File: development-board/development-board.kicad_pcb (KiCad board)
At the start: 2 copper layers, 153 x 77 mm, 103 parts, among them J1 East, J10 Ext_5V, J2 Screw_Terminal, J3 USB_B, J4 Keyboard, J5 Mouse, J6 Audio, J7 VGA, J8 West, J9 PinOut, Q1 MMBT3904, Q2 MMBT3904, Q3 S8050, Q4 S8050, SW1 Reset, SW2 Setup, SW3 Power, U1 LD1117S33, U2 FT2232HL, U3 93C46-WMN6TP, U4 LTV-817S, U5 LTV-817S, U6 MAX3486, U7 SN74CBT16292, U8 SN74CBT16292, Y1 12MHz

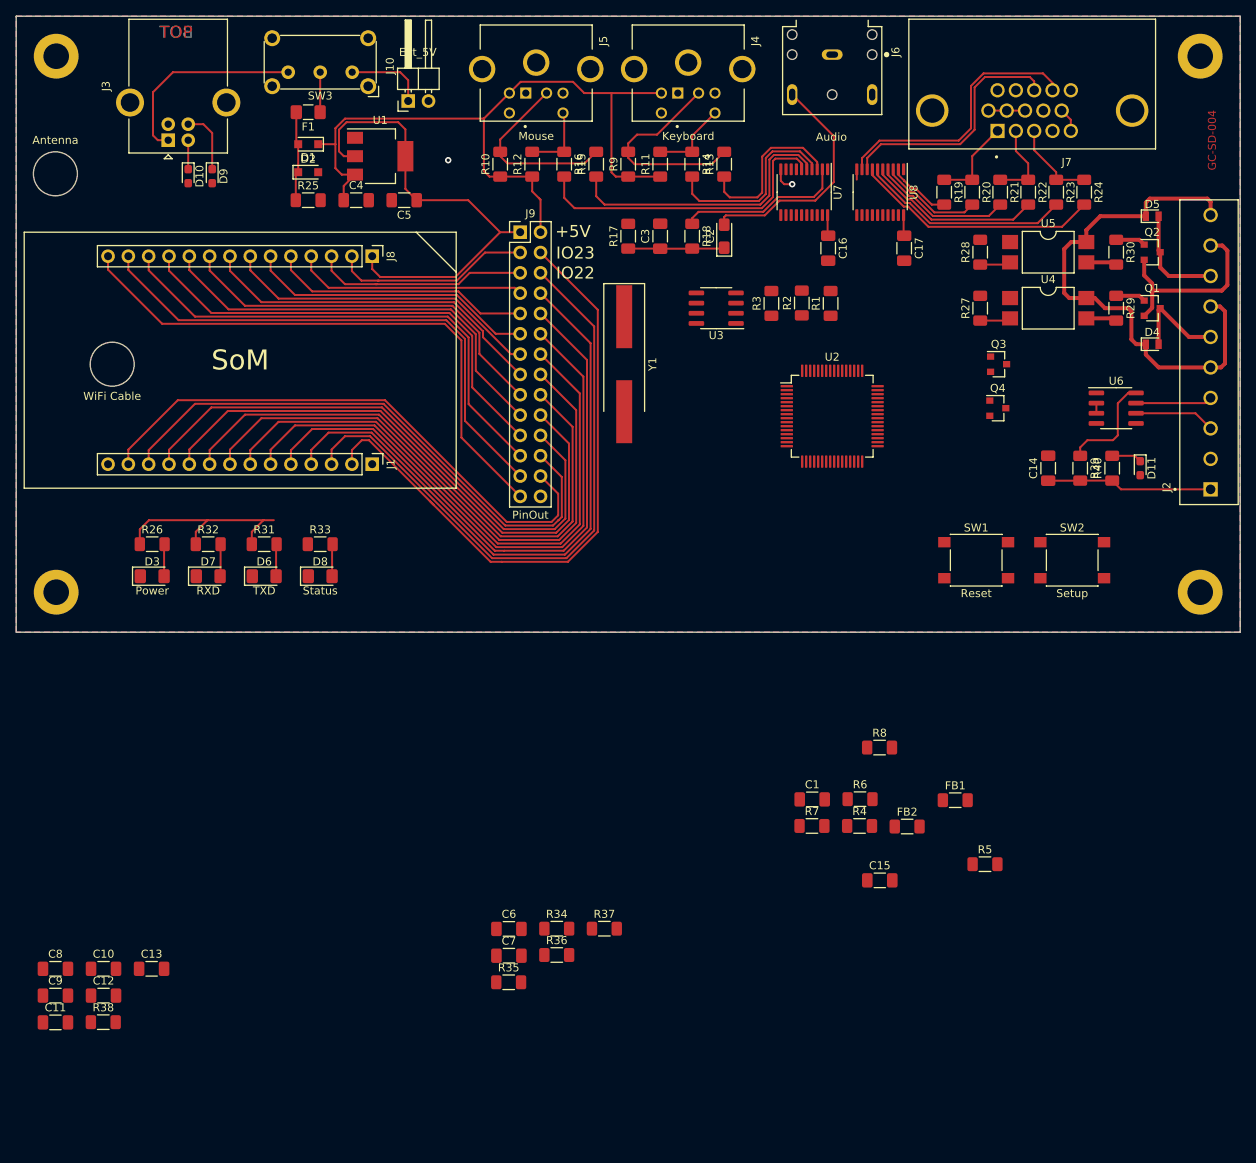
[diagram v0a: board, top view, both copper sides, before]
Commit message: Introduce new serial numbering scheme
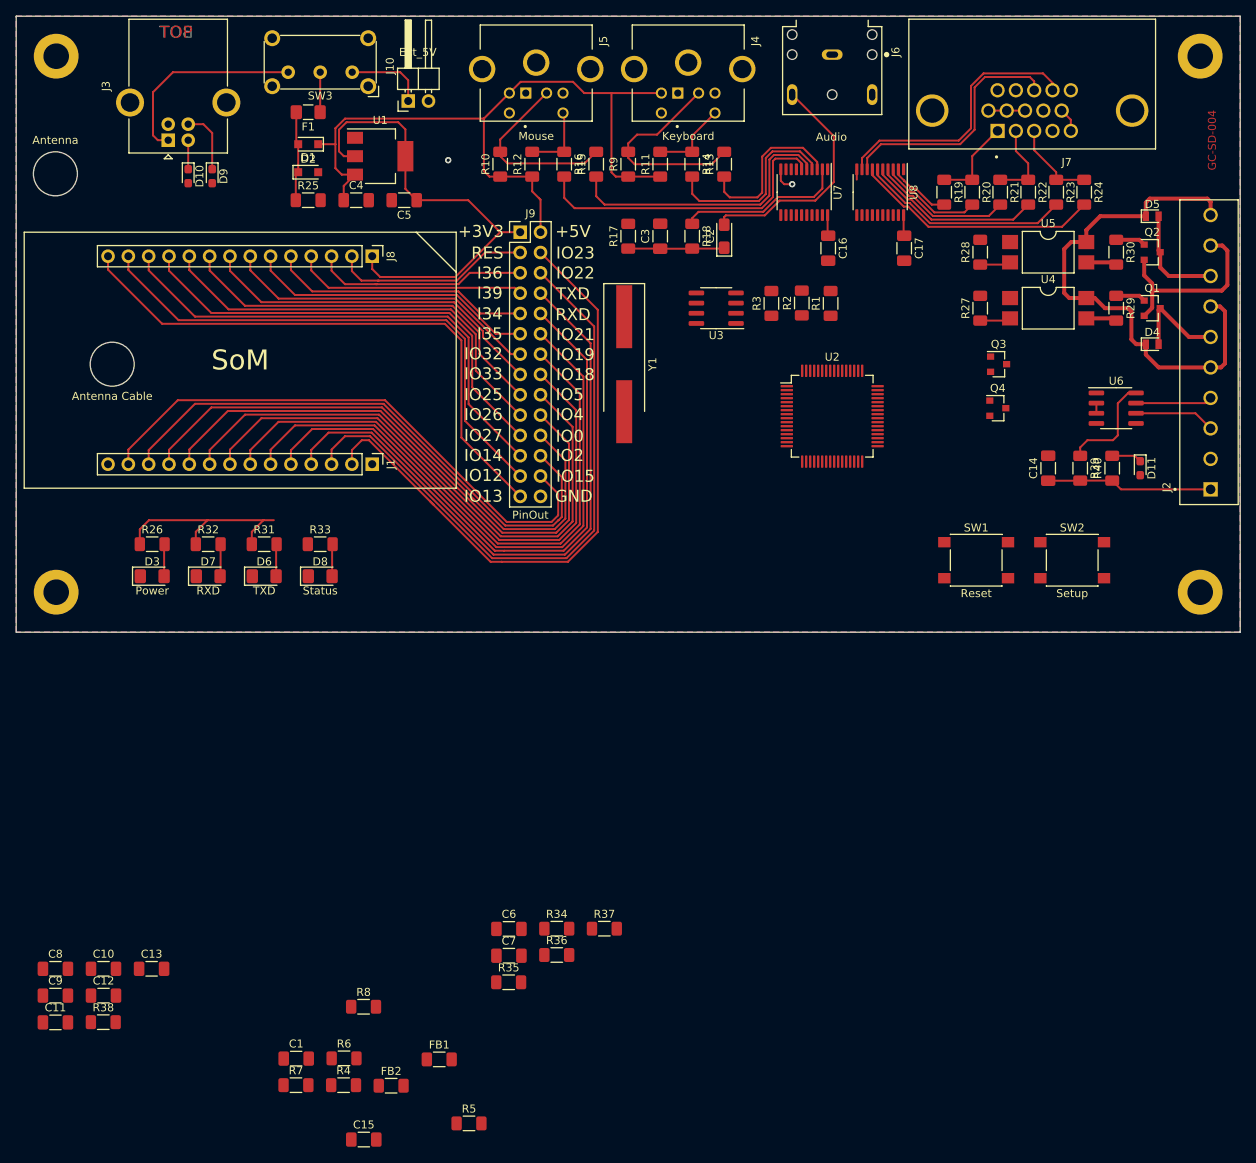
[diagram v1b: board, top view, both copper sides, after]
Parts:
- H5: value WiFi Cable -> Antenna Cable
- moved C1 72.2 mm to (85.0, 180.3)
- moved FB1 72.2 mm to (102.9, 180.4)
- moved FB2 72.2 mm to (96.9, 183.7)
- moved R5 72.2 mm to (106.6, 188.4)
- moved R7 72.2 mm to (85.0, 183.6)
- moved R4 72.2 mm to (90.9, 183.6)
- moved R6 72.2 mm to (91.0, 180.3)
- moved R8 72.2 mm to (93.4, 173.8)
- moved C15 72.2 mm to (93.5, 190.4)
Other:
- board text added: "+3V3"
- board text added: "GND"
- board text added: "I34"
- board text added: "I35"
- board text added: "I36"
- board text added: "I39"
- board text added: "IO0"
- board text added: "IO12"
- board text added: "IO13"
- board text added: "IO14"
- board text added: "IO15"
- board text added: "IO18"
- board text added: "IO19"
- board text added: "IO2"
- board text added: "IO21"
- board text added: "IO25"
- board text added: "IO26"
- board text added: "IO27"
- board text added: "IO32"
- board text added: "IO33"
- board text added: "IO4"
- board text added: "IO5"
- board text added: "RES"
- board text added: "RXD"
- board text added: "TXD"

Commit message: Feature/kicad 6 migration (#2)
* Adjust CI/CD jobs to use KiCad 6

* Migrate panel module project

* Unify KiBot config

* Migrate Ethernet, SoC, Metering Modules to KiCad6

* Change build order to find out more about strange behavior

* Trigger build also on workflow changes

* Try to increase log level to track error

* Switch to KiCad 6 schematic files

* Fix / Ignore Errors in panel module

* Disable cost calculation for now

* Fixing more ERC errors

* Remove outdated files and settings

* Trim further warnings and errors

* Update documentation

* Migrate in-progress projects
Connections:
- net FT_~DTR~ renamed FT_~{DTR}
- net FT_~RTS~ renamed FT_~{RTS}
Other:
- net class Default removed
